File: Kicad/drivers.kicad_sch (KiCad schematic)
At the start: 5 parts, among them U2 DRV8833PWP

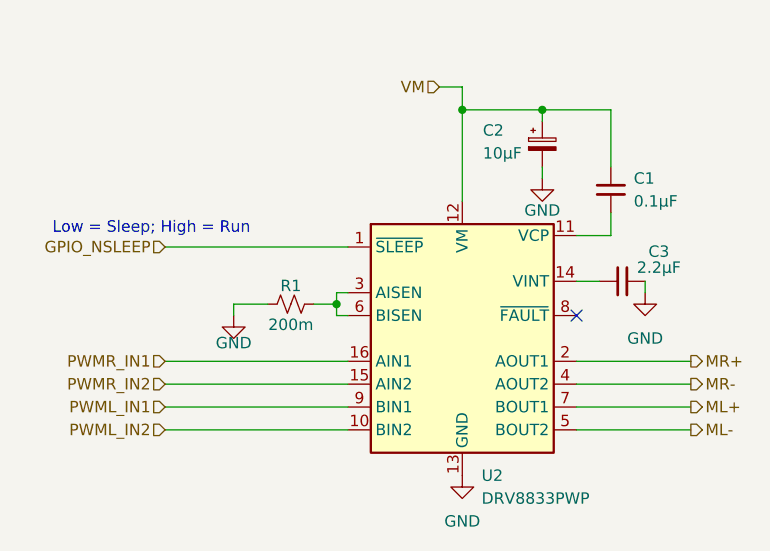
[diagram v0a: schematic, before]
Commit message: Feat: Added power LEDs 5v and 3v, Added Jumpers to battery and bms, Added segmentation in connector sheet, Added encoders, Changed page name from motor diver right to motor driver, Redid annotations, Changed output organisation on stm to match new ioc
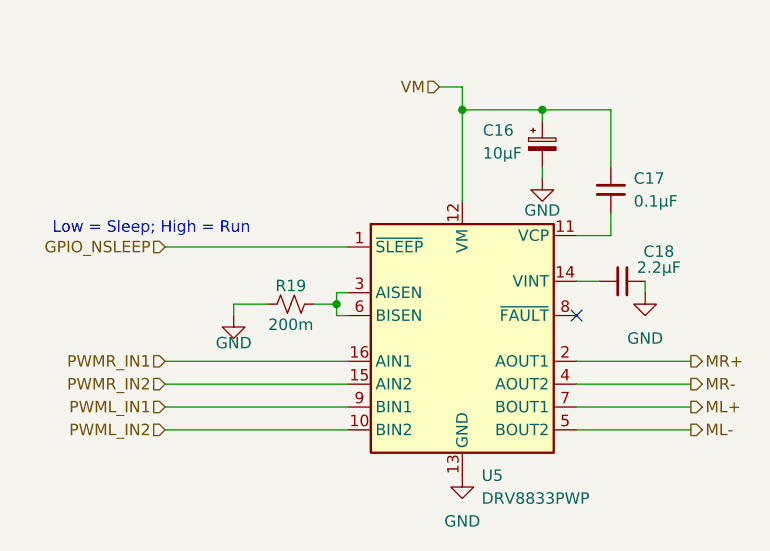
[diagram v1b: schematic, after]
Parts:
- renumbered C2 to C16, C1 to C17, C3 to C18, R1 to R19, U2 to U5
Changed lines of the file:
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@@
 		(dnp no)
 		(fields_autoplaced yes)
-		(property "Reference" "C1"
+		(property "Reference" "C17"
 			(at 123.19 36.8299 0)
 			(show_name no)
@@
 			(project "Redoubot"
 				(path "/43131b41-4104-4cd6-9c2f-4d5da1687300/b7c7d3a9-6fc5-4331-a1be-dcf952831da1"
-					(reference "C1")
+					(reference "C17")
 					(unit 1)
 				)
@@
 		(in_pos_files yes)
 		(dnp no)
-		(property "Reference" "R1"
+		(property "Reference" "R19"
 			(at 85.09 48.768 90)
 			(show_name no)
@@
 			(project "Redoubot"
 				(path "/43131b41-4104-4cd6-9c2f-4d5da1687300/b7c7d3a9-6fc5-4331-a1be-dcf952831da1"
-					(reference "R1")
+					(reference "R19")
 					(unit 1)
 				)
@@
 		(in_pos_files yes)
 		(dnp no)
-		(property "Reference" "#PWR02"
+		(property "Reference" "#PWR022"
 			(at 78.74 58.42 0)
 			(hide yes)
@@
 			(project "Redoubot"
 				(path "/43131b41-4104-4cd6-9c2f-4d5da1687300/b7c7d3a9-6fc5-4331-a1be-dcf952831da1"
-					(reference "#PWR02")
+					(reference "#PWR022")
 					(unit 1)
 				)
@@
 		(dnp no)
 		(fields_autoplaced yes)
-		(property "Reference" "U2"
+		(property "Reference" "U5"
 			(at 106.2833 69.85 0)
 			(show_name no)
@@
 			(project "Redoubot"
 				(path "/43131b41-4104-4cd6-9c2f-4d5da1687300/b7c7d3a9-6fc5-4331-a1be-dcf952831da1"
-					(reference "U2")
+					(reference "U5")
 					(unit 1)
 				)
@@
 		(in_pos_files yes)
 		(dnp no)
-		(property "Reference" "C3"
+		(property "Reference" "C18"
 			(at 125.984 44.958 90)
 			(show_name no)
@@
 			(project "Redoubot"
 				(path "/43131b41-4104-4cd6-9c2f-4d5da1687300/b7c7d3a9-6fc5-4331-a1be-dcf952831da1"
-					(reference "C3")
+					(reference "C18")
 					(unit 1)
 				)
@@
 		(in_pos_files yes)
 		(dnp no)
-		(property "Reference" "#PWR03"
+		(property "Reference" "#PWR024"
 			(at 113.03 43.18 0)
 			(hide yes)
@@
 			(project "Redoubot"
 				(path "/43131b41-4104-4cd6-9c2f-4d5da1687300/b7c7d3a9-6fc5-4331-a1be-dcf952831da1"
-					(reference "#PWR03")
+					(reference "#PWR024")
 					(unit 1)
 				)
@@
 		(dnp no)
 		(fields_autoplaced yes)
-		(property "Reference" "#PWR04"
+		(property "Reference" "#PWR025"
 			(at 124.46 55.88 0)
 			(hide yes)
@@
 			(project "Redoubot"
 				(path "/43131b41-4104-4cd6-9c2f-4d5da1687300/b7c7d3a9-6fc5-4331-a1be-dcf952831da1"
-					(reference "#PWR04")
+					(reference "#PWR025")
 					(unit 1)
 				)
@@
 		(in_pos_files yes)
 		(dnp no)
-		(property "Reference" "C2"
+		(property "Reference" "C16"
 			(at 106.426 31.496 0)
 			(show_name no)
@@
 			(project "Redoubot"
 				(path "/43131b41-4104-4cd6-9c2f-4d5da1687300/b7c7d3a9-6fc5-4331-a1be-dcf952831da1"
-					(reference "C2")
+					(reference "C16")
 					(unit 1)
 				)
@@
 		(dnp no)
 		(fields_autoplaced yes)
-		(property "Reference" "#PWR011"
+		(property "Reference" "#PWR023"
 			(at 104.14 76.2 0)
 			(hide yes)
@@
 			(project "Redoubot"
 				(path "/43131b41-4104-4cd6-9c2f-4d5da1687300/b7c7d3a9-6fc5-4331-a1be-dcf952831da1"
-					(reference "#PWR011")
-					(unit 1)
-				)
+					(reference "#PWR023")
+					(unit 1)
+				)

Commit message: feat: changed the footprints to 1206 for the shunt resistors R18 and R19 and put a JST connector footprint for the Bluetooth Module
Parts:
- R19: footprint Resistor_SMD:R_0402_1005Metric -> Resistor_SMD:R_1206_3216Metric
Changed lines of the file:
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@@
 			)
 		)
-		(property "Footprint" "Resistor_SMD:R_0402_1005Metric"
+		(property "Footprint" "Resistor_SMD:R_1206_3216Metric"
 			(at 85.09 50.8 0)
 			(hide yes)

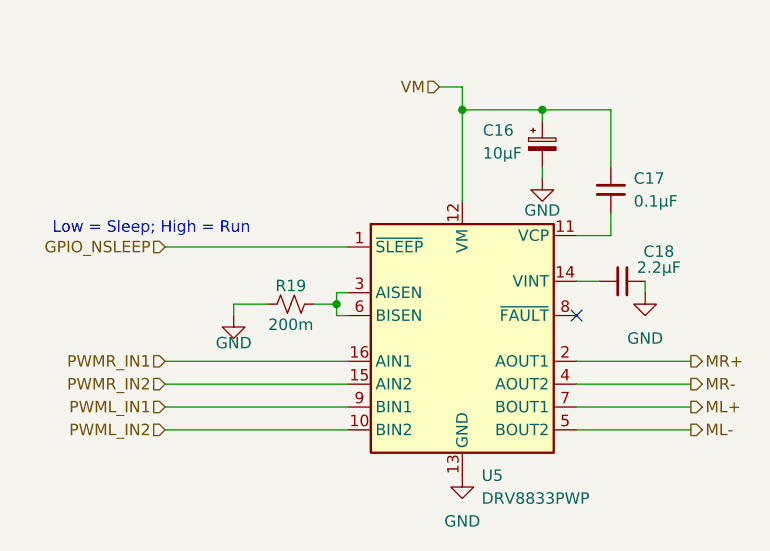
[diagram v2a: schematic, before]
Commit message: feat: added power flags, no errors during ERC
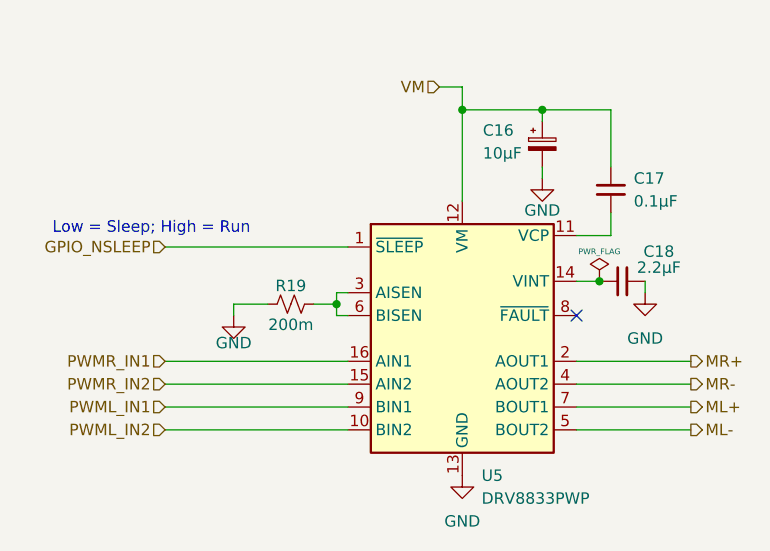
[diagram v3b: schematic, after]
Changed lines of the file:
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@@
+	)
+	(junction
+		(at 119.38 48.26)
+		(diameter 0)
+		(color 0 0 0 0)
 	)
 	(junction
@@
 					(unit 1)
 				)
+			)
+		)
+	)
+	(symbol
+		(lib_id "power:PWR_FLAG")
+		(at 119.38 48.26 0)
+		(unit 1)
+		(body_style 1)
+		(exclude_from_sim no)
+		(in_bom yes)
+		(on_board yes)
+		(in_pos_files yes)
+		(dnp no)
+		(property "Reference" "#FLG09"
+			(at 119.38 46.355 0)
+			(hide yes)
+			(show_name no)
+			(do_not_autoplace no)
+			(effects
+				(font
+					(size 1.27 1.27)
+				)
+			)
+		)
+		(property "Value" "PWR_FLAG"
+			(at 119.38 44.958 0)
+			(show_name no)
+			(do_not_autoplace no)
+			(effects
+				(font
+					(size 0.635 0.635)
+				)
+			)
+		)
+		(property "Footprint" ""
+			(at 119.38 48.26 0)
+			(hide yes)
+			(show_name no)
+			(do_not_autoplace no)
+			(effects
+				(font
+					(size 1.27 1.27)
+				)
+			)
+		)
+		(property "Datasheet" ""
+			(at 119.38 48.26 0)
+			(hide yes)
+			(show_name no)
+			(do_not_autoplace no)
+			(effects
+				(font
+					(size 1.27 1.27)
+				)
+			)
+		)
+		(property "Description" "Special symbol for telling ERC where power comes from"
+			(at 119.38 48.26 0)
+			(hide yes)
+			(show_name no)
+			(do_not_autoplace no)
+			(effects
+				(font
+					(size 1.27 1.27)
+				)
+			)
+		)
+		(pin "1"
+		)
+		(instances
+			(project "Redoubot"
+				(path "/43131b41-4104-4cd6-9c2f-4d5da1687300/b7c7d3a9-6fc5-4331-a1be-dcf952831da1"
+					(reference "#FLG09")
+					(unit 1)
+				)

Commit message: feat: electrical schematic validated
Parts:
- added C29: 10u/25V, Capacitor_SMD:C_0603_1608Metric, symbol Device:C_Small
- added R22: 200m, Resistor_SMD:R_1206_3216Metric, symbol Device:R_Small_US
- C16: value 10µF -> 470u/25V; footprint Capacitor_SMD:CP_Elec_4x5.4 -> Capacitor_SMD:CP_Elec_10x10.5
- C17: value 0.1µF -> 10n
- C18: value 2.2µF -> 2u2; footprint Capacitor_SMD:C_0603_1608Metric -> Capacitor_SMD:C_0402_1005Metric
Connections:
- net GND: now also C29.2, R22.1
- net at R19.2, U5.3 (AISEN): no longer U5.6 (BISEN)
- net VM renamed +5V
- net +5V: now also C29.1
- new net: R22.2, U5.6 (BISEN)
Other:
- moved on the sheet: C16, R19

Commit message: feat: added the footprints for new components and started assigning the JLCPCB part numbers
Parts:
- C16: footprint Capacitor_SMD:CP_Elec_10x10.5 -> Capacitor_SMD:CP_Elec_8x10.5; JLCPCB Part # (none) -> C48935394
- C17: JLCPCB Part # (none) -> C15195
- C18: JLCPCB Part # (none) -> C12530
- C29: JLCPCB Part # (none) -> C96446
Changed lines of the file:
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@@
+			)
+		)
+		(property "JLCPCB Part #" "C15195"
+			(at 120.65 38.1 0)
+			(hide yes)
+			(show_name no)
+			(do_not_autoplace no)
+			(effects
+				(font
+					(size 1.27 1.27)
+				)
 			)
 		)
@@
 			)
 		)
+		(property "JLCPCB Part #" "C12530"
+			(at 121.92 48.26 90)
+			(hide yes)
+			(show_name no)
+			(do_not_autoplace no)
+			(effects
+				(font
+					(size 1.27 1.27)
+				)
+			)
+		)
 		(pin "1"
 		)
@@
 			)
 		)
+		(property "JLCPCB Part #" "C96446"
+			(at 87.63 33.02 0)
+			(hide yes)
+			(show_name no)
+			(do_not_autoplace no)
+			(effects
+				(font
+					(size 1.27 1.27)
+				)
+			)
+		)
 		(pin "2"
 		)
@@
 			)
 		)
-		(property "Footprint" "Capacitor_SMD:CP_Elec_10x10.5"
+		(property "Footprint" "Capacitor_SMD:CP_Elec_8x10.5"
 			(at 76.2 33.02 0)
 			(hide yes)
@@
 			(at 76.2 33.02 0)
 			(hide yes)
+			(show_name no)
+			(do_not_autoplace no)
+			(effects
+				(font
+					(size 1.27 1.27)
+				)
+			)
+		)
+		(property "JLCPCB Part #" "C48935394"
+			(at 76.2 33.02 0)
+			(hide yes)
